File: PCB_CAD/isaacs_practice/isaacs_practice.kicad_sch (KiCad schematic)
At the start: 1 part, among them U1 DIX9211PTR

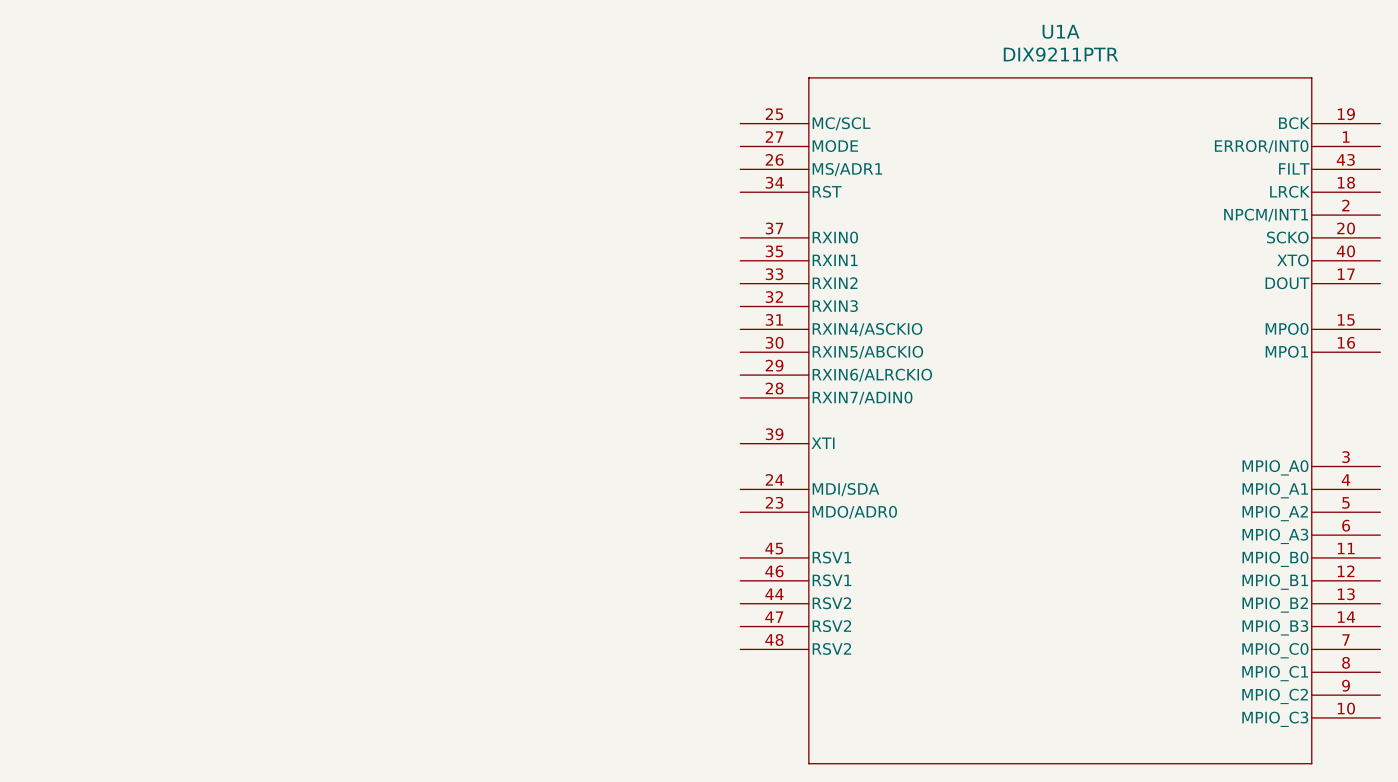
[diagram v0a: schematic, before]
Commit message: schematic add NAU8402WG DAC
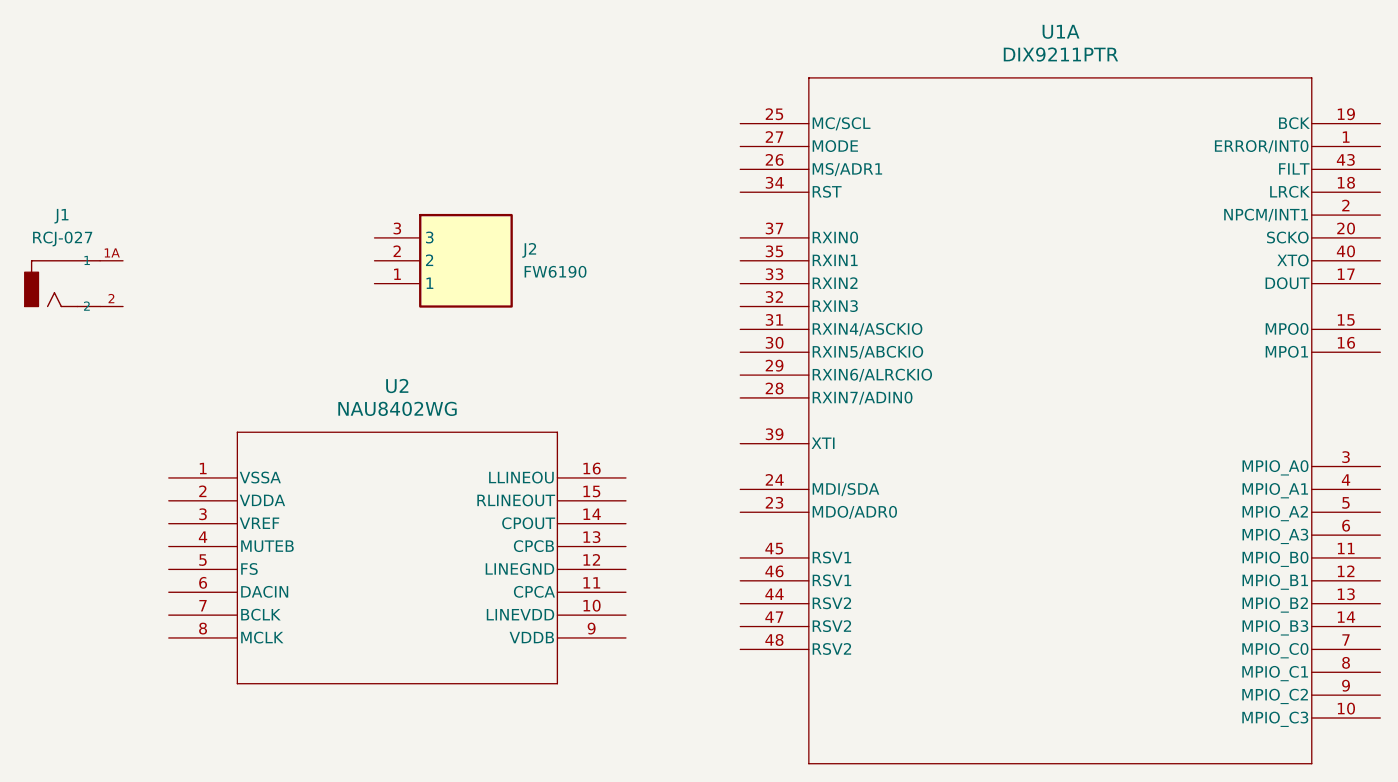
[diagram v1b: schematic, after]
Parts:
- added J1: RCJ-027, RCJ-027:CUI_RCJ-027, symbol RCJ-027:RCJ-027
- added J2: FW6190, FW6190, symbol FW6190:FW6190
- added U2: NAU8402WG, TSSOP16_NAU8402_NUV, symbol NAU8402WG:NAU8402WG
